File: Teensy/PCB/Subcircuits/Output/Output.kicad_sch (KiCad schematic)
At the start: 5 parts

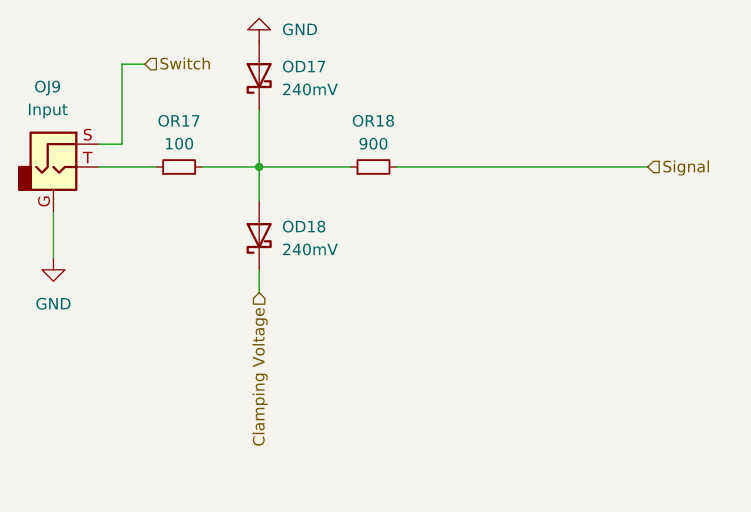
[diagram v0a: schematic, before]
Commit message: Replaced Schematic Lines with references
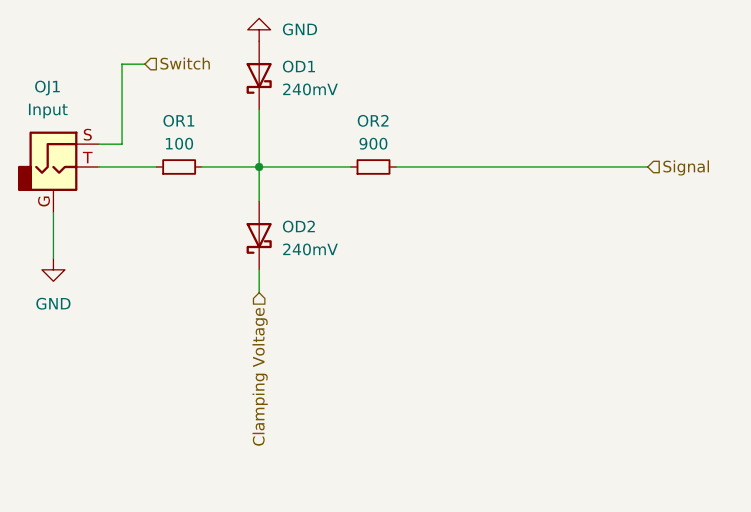
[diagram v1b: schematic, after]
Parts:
- renumbered OD17 to OD1, OD18 to OD2, OJ9 to OJ1, OR17 to OR1, OR18 to OR2
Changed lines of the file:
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@@
   (symbol (lib_id "Device:D_Schottky") (at 102.87 96.52 90) (unit 1)
     (in_bom yes) (on_board yes) (fields_autoplaced)
-    (property "Reference" "OD18" (id 0) (at 105.41 95.5674 90)
+    (property "Reference" "OD2" (id 0) (at 105.41 95.5674 90)
       (effects (font (size 1.27 1.27)) (justify right))
     )
@@
   (symbol (lib_id "Connector:AudioJack2_Ground") (at 80.01 88.9 0) (unit 1)
     (in_bom yes) (on_board yes) (fields_autoplaced)
-    (property "Reference" "OJ9" (id 0) (at 79.375 80.01 0))
+    (property "Reference" "OJ1" (id 0) (at 79.375 80.01 0))
     (property "Value" "Input" (id 1) (at 79.375 82.55 0))
     (property "Footprint" "Perfboard:3.5mm Jack Perfboard" (id 2) (at 80.01 88.9 0)
@@
   (symbol (lib_id "Device:D_Schottky") (at 102.87 78.74 90) (unit 1)
     (in_bom yes) (on_board yes) (fields_autoplaced)
-    (property "Reference" "OD17" (id 0) (at 105.41 77.7874 90)
+    (property "Reference" "OD1" (id 0) (at 105.41 77.7874 90)
       (effects (font (size 1.27 1.27)) (justify right))
     )
@@
   (symbol (lib_id "power:GND") (at 80.01 99.06 0) (unit 1)
     (in_bom yes) (on_board yes) (fields_autoplaced)
-    (property "Reference" "#PWR0163" (id 0) (at 80.01 105.41 0)
+    (property "Reference" "#PWR030" (id 0) (at 80.01 105.41 0)
       (effects (font (size 1.27 1.27)) hide)
     )
@@
   (symbol (lib_id "Device:R_Small") (at 93.98 88.9 90) (unit 1)
     (in_bom yes) (on_board yes)
-    (property "Reference" "OR17" (id 0) (at 93.98 83.82 90))
+    (property "Reference" "OR1" (id 0) (at 93.98 83.82 90))
     (property "Value" "100" (id 1) (at 93.98 86.36 90))
     (property "Footprint" "Resistor_SMD:R_1206_3216Metric_Pad1.30x1.75mm_HandSolder" (id 2) (at 93.98 88.9 0)
@@
   (symbol (lib_id "power:GND") (at 102.87 74.93 180) (unit 1)
     (in_bom yes) (on_board yes) (fields_autoplaced)
-    (property "Reference" "#PWR0164" (id 0) (at 102.87 68.58 0)
+    (property "Reference" "#PWR031" (id 0) (at 102.87 68.58 0)
       (effects (font (size 1.27 1.27)) hide)
     )
@@
   (symbol (lib_id "Device:R_Small") (at 115.57 88.9 90) (unit 1)
     (in_bom yes) (on_board yes)
-    (property "Reference" "OR18" (id 0) (at 115.57 83.82 90))
+    (property "Reference" "OR2" (id 0) (at 115.57 83.82 90))
     (property "Value" "900" (id 1) (at 115.57 86.36 90))
     (property "Footprint" "Resistor_SMD:R_1206_3216Metric_Pad1.30x1.75mm_HandSolder" (id 2) (at 115.57 88.9 0)
